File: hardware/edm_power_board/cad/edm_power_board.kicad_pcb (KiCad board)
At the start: 4 copper layers, 240 x 100 mm, 158 parts, among them J501 Conn_02x08_Odd_Even, J502 Conn_01x02, Q201 SUD19P06-60, Q301 BSS214NW, Q302 BSC13DN30NSFD, Q303 BSS214NW, Q304 BSS214NW, Q601 IPD50R3K0CE, Q602 IPD50R380CE, U201 LM358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

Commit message: Update bleed resistor
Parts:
- removed MK506, MK512: Mounting_Hole_PAD, MountingHole:MountingHole_5mm_Pad
- added R623: 187k, Resistor_SMD:R_0805_2012Metric, F.Cu at (225.0, -9.96)
- added R624: 187k, Resistor_SMD:R_0805_2012Metric, F.Cu at (225.0, -6.04)
- C315, C316: value 25u -> 470n; footprint Capacitor_THT:C_Rect_L41.5mm_W20.0mm_P37.50mm_MKS4 -> Capacitor_SMD:C_1812_4532Metric
- R308, R316: value 261R -> 26k1
- R313: value 523R -> 52k3
- R317: value 21k -> 2M1
- R318: value 180R -> 18k
- R612, R618: value 10k -> 21k
- R613, R614, R619, R620: value 93k1 -> 187k
- RV601: value 50k -> 100k
- RV602: value 250k -> 500k
- moved C316 22.0 mm to (137.0, -63.8), turned to 270 degrees
- moved C315 21.2 mm to (131.0, -63.8), turned to 270 degrees
- moved R216 2.00 mm to (158.9, -30.0)
- moved R220 2.00 mm to (166.6, -30.0)
- moved R221 2.00 mm to (162.7, -30.0)
- moved C602 2.00 mm to (182.3, -14.2)
- moved C608 2.00 mm to (114.7, -6.37)
- moved C201 2.00 mm to (155.2, -30.0)
- moved C202 2.00 mm to (147.6, -29.9)
- moved C203 2.00 mm to (141.7, -42.4)
- moved C204 2.00 mm to (147.0, -43.2)
- moved C205 2.00 mm to (142.3, -29.3)
- moved C206 2.00 mm to (146.5, -23.0)
- moved C207 2.00 mm to (148.9, -37.5)
- moved C208 2.00 mm to (155.2, -37.5)
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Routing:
- net GNDPWR: track 212.4 -> 232.3 mm, vias 108 -> 117
- net Net-(R623-Pad1): track 0.00 -> 2.00 mm
- net Net-(C310-Pad2): track 0.00 -> 1.59 mm
- net Net-(Q304-Pad1): track 65.1 -> 64.3 mm
- net Net-(R304-Pad2): track 86.6 -> 85.8 mm
- net +5V: track 165.8 -> 165.0 mm
- net Net-(U601-Pad14): track 185.6 -> 184.8 mm
- net Net-(U601-Pad13): track 152.7 -> 151.8 mm
- net Net-(R615-Pad1): track 74.7 -> 73.8 mm
- net Net-(R606-Pad1): track 97.5 -> 96.7 mm
- net Net-(Q303-Pad1): track 64.4 -> 63.6 mm
- net Net-(Q301-Pad1): track 63.9 -> 63.1 mm
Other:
- board size 240 x 100 mm -> 240 x 80 mm

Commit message: Rotate board
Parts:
- removed MK505, MK511: Mounting_Hole_PAD, MountingHole:MountingHole_5mm_Pad
- moved MK501 235.0 mm to (234.4, -63.8), turned to 180 degrees
- moved MK507 235.0 mm to (5.60, -63.8), turned to 180 degrees
- moved MK504 232.6 mm to (234.4, -16.2), turned to 180 degrees
- moved MK510 232.6 mm to (5.60, -16.2), turned to 180 degrees
- moved MK502 229.8 mm to (234.4, -47.9), turned to 180 degrees
- moved MK508 229.8 mm to (5.60, -47.9), turned to 180 degrees
- moved MK503 229.0 mm to (234.4, -32.1), turned to 180 degrees
- moved MK509 229.0 mm to (5.60, -32.1), turned to 180 degrees
- moved R624 220.7 mm to (15.0, -74.0), turned to 270 degrees
- moved R623 218.4 mm to (15.0, -70.0), turned to 270 degrees
- moved JJ503 207.2 mm to (20.0, -13.0), turned to 0 degrees
- moved D607 200.8 mm to (23.0, -66.0), turned to 0 degrees
- moved R619 193.2 mm to (30.0, -75.0), turned to 180 degrees
- moved J501 192.4 mm to (215.5, -51.4), turned to 180 degrees
- moved R613 191.1 mm to (30.0, -72.0), turned to 180 degrees
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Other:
- outline, holes or cut-outs redrawn
- board text added: "+24V"
- board text added: "0V"
- board text added: "1"
- board text added: "Breakdown"
- board text added: "Out+"
- board text added: "Out-"
- board text added: "Short circuit"
- board text added: "Spark voltage"

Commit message: Routing
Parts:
- added C501: 1800p, Capacitor_SMD:C_2220_5650Metric, F.Cu at (220.5, -16.0)
- added R501: 1M, Resistor_SMD:R_1206_3216Metric, F.Cu at (220.5, -24.0)
- moved R623 3.16 mm to (18.0, -71.0)
- moved R624 3.16 mm to (18.0, -75.0)
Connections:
- MK501 pad 1: GNDPWR -> /Connectors/Shield
- MK502 pad 1: GNDPWR -> /Connectors/Shield
- MK503 pad 1: GNDPWR -> /Connectors/Shield
- MK504 pad 1: GNDPWR -> /Connectors/Shield
- MK507 pad 1: GNDPWR -> /Connectors/Shield
- MK508 pad 1: GNDPWR -> /Connectors/Shield
- MK509 pad 1: GNDPWR -> /Connectors/Shield
- MK510 pad 1: GNDPWR -> /Connectors/Shield
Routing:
- net /Connectors/Shield: track 0.00 -> 27.1 mm
- net GNDPWR: track 232.3 -> 246.2 mm, vias 117 -> 121
- added copper zone on B.Cu, net /Connectors/Shield
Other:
- board text added: "EDM Power Board 2018-02-18 JS"
- board text added: "EDM current"
- board text removed: "Spark voltage"

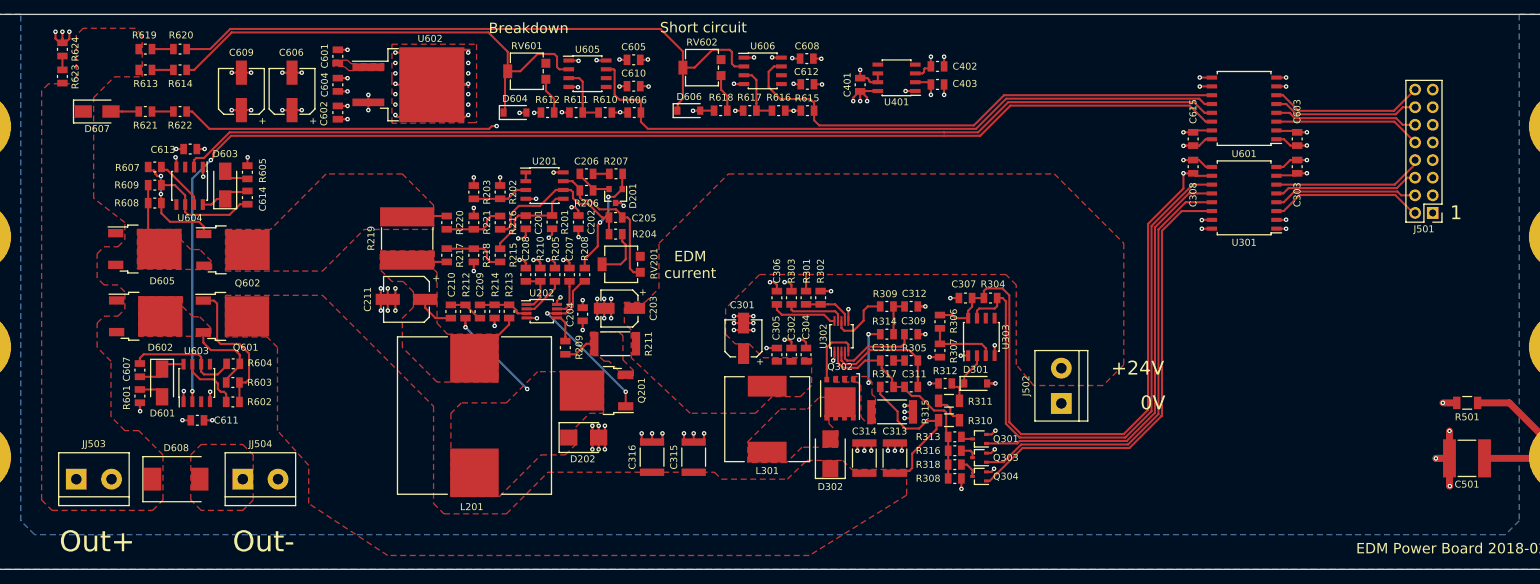
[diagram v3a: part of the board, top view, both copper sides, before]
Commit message: Added copper planes to front and back. Added gerber files.
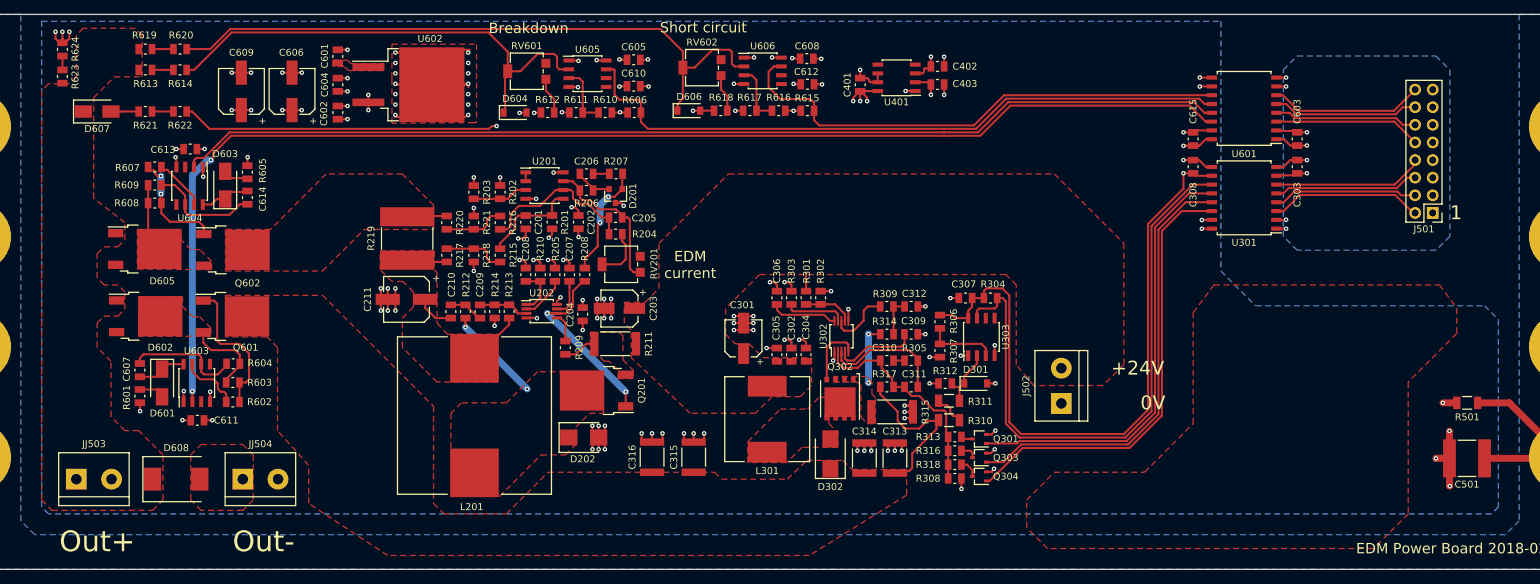
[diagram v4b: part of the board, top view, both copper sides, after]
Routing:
- added copper zone on F.Cu, net (none)
- added copper zone on B.Cu, net GND
- added copper zone on B.Cu, net GNDPWR
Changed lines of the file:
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@@
     (thickness 1.6)
     (drawings 13)
-    (tracks 1160)
+    (tracks 1161)
     (zones 0)
     (modules 158)
@@
     (31 B.Cu signal hide)
     (32 B.Adhes user hide)
-    (33 F.Adhes user)
-    (34 B.Paste user)
-    (35 F.Paste user)
-    (36 B.SilkS user)
-    (37 F.SilkS user)
-    (38 B.Mask user)
-    (39 F.Mask user)
-    (40 Dwgs.User user)
-    (41 Cmts.User user)
-    (42 Eco1.User user)
-    (43 Eco2.User user)
+    (33 F.Adhes user hide)
+    (34 B.Paste user hide)
+    (35 F.Paste user hide)
+    (36 B.SilkS user hide)
+    (37 F.SilkS user hide)
+    (38 B.Mask user hide)
+    (39 F.Mask user hide)
+    (40 Dwgs.User user hide)
+    (41 Cmts.User user hide)
+    (42 Eco1.User user hide)
+    (43 Eco2.User user hide)
     (44 Edge.Cuts user)
-    (45 Margin user)
-    (46 B.CrtYd user)
-    (47 F.CrtYd user)
-    (48 B.Fab user)
-    (49 F.Fab user)
+    (45 Margin user hide)
+    (46 B.CrtYd user hide)
+    (47 F.CrtYd user hide)
+    (48 B.Fab user hide)
+    (49 F.Fab user hide)
   )
   (setup
@@
       (outputformat 1)
       (mirror false)
-      (drillshape 1)
+      (drillshape 0)
       (scaleselection 1)
-      (outputdirectory ""))
+      (outputdirectory ../documents/gerber/))
   )
   (net 0 "")
@@
   (segment (start 37.3 -59.3) (end 36.966965 -58.966965) (width 0.3) (layer F.Cu) (net 30))
   (segment (start 36.966965 -58.966965) (end 36.966965 -57.988462) (width 0.3) (layer F.Cu) (net 30))
+  (segment (start 39.4 -59) (end 38.940381 -59) (width 1) (layer B.Cu) (net 31))
+  (segment (start 38.940381 -59) (end 36.72999 -56.789609) (width 1) (layer B.Cu) (net 31))
+  (segment (start 36.72999 -56.789609) (end 36.72999 -26.129629) (width 1) (layer B.Cu) (net 31))
+  (segment (start 36.72999 -26.129629) (end 36.72999 -25.67001) (width 1) (layer B.Cu) (net 31))
   (segment (start 154.64997 -66.84997) (end 180.5 -66.84997) (width 0.3) (layer F.Cu) (net 31))
   (segment (start 145.10001 -62.49999) (end 150.29999 -62.49999) (width 0.3) (layer F.Cu) (net 31))
@@
   (via (at 39.4 -59) (size 0.65) (drill 0.3) (layers F.Cu B.Cu) (net 31))
   (via (at 36.72999 -25.67001) (size 0.65) (drill 0.3) (layers F.Cu B.Cu) (net 31))
-  (segment (start 36.72999 -25.67001) (end 36.72999 -56.32999) (width 0.3) (layer B.Cu) (net 31))
-  (segment (start 36.72999 -56.32999) (end 39.4 -59) (width 0.3) (layer B.Cu) (net 31))
   (segment (start 36.72999 -24.173646) (end 36.72999 -25.67001) (width 0.3) (layer F.Cu) (net 31))
   (segment (start 128.700183 -35.799817) (end 127.8 -36.7) (width 0.3) (layer F.Cu) (net 42))
@@
   (segment (start 144.5 -23.7) (end 144.3 -23.9) (width 0.3) (layer F.Cu) (net 53))
   (segment (start 144.3 -23.9) (end 144.3 -24.3) (width 0.3) (layer F.Cu) (net 53))
+  (segment (start 87.9 -36.9) (end 99.2 -25.6) (width 1) (layer B.Cu) (net 61))
   (segment (start 83.734606 -50.998433) (end 83.2 -50.463827) (width 0.3) (layer F.Cu) (net 63))
   (segment (start 84.784606 -50.998433) (end 83.734606 -50.998433) (width 0.3) (layer F.Cu) (net 63))
@@
   (segment (start 89.122173 -54.687481) (end 86.834692 -52.4) (width 0.3) (layer F.Cu) (net 65))
   (segment (start 82.122481 -49.022481) (end 81.097173 -49.022481) (width 0.3) (layer F.Cu) (net 65))
+  (segment (start 95.5 -50) (end 95.5 -52.5) (width 1) (layer B.Cu) (net 70))
+  (segment (start 95.5 -52.5) (end 96.7 -53.7) (width 1) (layer B.Cu) (net 70))
+  (segment (start 76.1 -34.9) (end 85 -26) (width 1) (layer B.Cu) (net 71))
   (segment (start 32.666965 -57.6) (end 33.1 -57.6) (width 0.3) (layer F.Cu) (net 80))
   (segment (start 32.266965 -58) (end 32.666965 -57.6) (width 0.3) (layer F.Cu) (net 80))
   (segment (start 33.1 -57.6) (end 36.966965 -53.733035) (width 0.3) (layer F.Cu) (net 80))
   (segment (start 36.966965 -53.733035) (end 36.966965 -52.588462) (width 0.3) (layer F.Cu) (net 80))
+  (segment (start 32.2 -56.7) (end 32.2 -54.1) (width 1) (layer B.Cu) (net 81))
   (segment (start 31.4 -57) (end 31.7 -56.7) (width 0.3) (layer F.Cu) (net 81))
   (segment (start 31.7 -56.7) (end 32.2 -56.7) (width 0.3) (layer F.Cu) (net 81))
@@
   (segment (start 32.2 -54.1) (end 32.2 -53.055427) (width 0.3) (layer F.Cu) (net 81))
   (segment (start 32.2 -53.055427) (end 32.266965 -52.988462) (width 0.3) (layer F.Cu) (net 81))
-  (segment (start 32.2 -56.7) (end 32.2 -54.1) (width 0.3) (layer B.Cu) (net 81))
   (via (at 32.2 -54.1) (size 0.65) (drill 0.3) (layers F.Cu B.Cu) (net 81))
   (via (at 32.2 -56.7) (size 0.65) (drill 0.3) (layers F.Cu B.Cu) (net 81))
@@
   (segment (start 26.55 -66) (end 29 -66) (width 0.3) (layer F.Cu) (net 90))
   (segment (start 30.91 -66) (end 34 -66) (width 0.3) (layer F.Cu) (net 91))
-  (segment (start 134.200001 -26.9) (end 134.200001 -33.899993) (width 0.3) (layer B.Cu) (net 93))
-  (segment (start 134.200001 -33.899993) (end 134.200008 -33.9) (width 0.3) (layer B.Cu) (net 93))
+  (segment (start 134.200001 -26.9) (end 134.200001 -33.899993) (width 1) (layer B.Cu) (net 93))
+  (segment (start 134.200001 -33.899993) (end 134.200008 -33.9) (width 1) (layer B.Cu) (net 93))
   (segment (start 134.200191 -33.899817) (end 134.200008 -33.9) (width 0.3) (layer F.Cu) (net 93))
   (segment (start 135.896959 -33.899817) (end 134.200191 -33.899817) (width 0.3) (layer F.Cu) (net 93))
@@
   (segment (start 99.2 -23.5) (end 99.2 -25.6) (width 0.3) (layer F.Cu) (net 61))
   (via (at 99.2 -25.6) (size 0.65) (drill 0.3) (layers F.Cu B.Cu) (net 61))
-  (segment (start 99.2 -25.6) (end 87.9 -36.9) (width 0.3) (layer B.Cu) (net 61))
   (segment (start 87.9 -36.9) (end 89.294654 -36.9) (width 0.3) (layer F.Cu) (net 61))
   (segment (start 89.294654 -36.9) (end 89.297173 -36.897481) (width 0.3) (layer F.Cu) (net 61))
@@
   (segment (start 95.175001 -46.575001) (end 95.175001 -49.675001) (width 0.3) (layer F.Cu) (net 70))
   (segment (start 95.175001 -49.675001) (end 95.5 -50) (width 0.3) (layer F.Cu) (net 70))
-  (segment (start 96.7 -53.7) (end 96.7 -51.2) (width 0.3) (layer B.Cu) (net 70))
-  (segment (start 96.7 -51.2) (end 95.824999 -50.324999) (width 0.3) (layer B.Cu) (net 70))
-  (segment (start 95.824999 -50.324999) (end 95.5 -50) (width 0.3) (layer B.Cu) (net 70))
   (via (at 95.5 -50) (size 0.65) (drill 0.3) (layers F.Cu B.Cu) (net 70))
   (segment (start 96.7 -53.7) (end 97.574692 -53.7) (width 0.3) (layer F.Cu) (net 70))
@@
   (segment (start 98.697173 -56.967481) (end 98.752173 -57.022481) (width 0.3) (layer F.Cu) (net 70))
   (segment (start 85 -26) (end 85.000004 -26) (width 0.3) (layer B.Cu) (net 71))
-  (segment (start 76.1 -34.9) (end 85 -26) (width 0.3) (layer B.Cu) (net 71))
   (via (at 85 -26) (size 0.65) (drill 0.3) (layers F.Cu B.Cu) (net 71))
   (segment (start 92.88 -25.8) (end 92.9 -25.78) (width 0.3) (layer F.Cu) (net 71))
@@
       )
     )
+  )
+  (zone (net 0) (net_name "") (layer F.Cu) (hatch edge 0.508)
+    (connect_pads (clearance 0.508))
+    (min_thickness 0.254)
+    (fill yes (arc_segments 16) (thermal_gap 0.508) (thermal_bridge_width 0.508))
+    (polygon
+      (pts
+        (xy 157 -6) (xy 157 -10) (xy 161 -14) (xy 174 -14) (xy 181 -21)
+        (xy 181 -37) (xy 184 -41) (xy 216.500002 -41) (xy 219 -37.666667) (xy 219 -34)
+        (xy 212 -27) (xy 212 -8) (xy 207 -3) (xy 160 -3)
+      )
+    )
+  )
+  (zone (net 1) (net_name GNDPWR) (layer B.Cu) (hatch edge 0.508)
+    (connect_pads (clearance 0.508))
+    (min_thickness 0.254)
+    (fill yes (arc_segments 16) (thermal_gap 0.508) (thermal_bridge_width 0.508))
+    (polygon
+      (pts
+        (xy 185 -43) (xy 190 -38) (xy 223 -38) (xy 225 -36) (xy 225 -9)
+        (xy 224 -8) (xy 16 -8) (xy 15 -9) (xy 15 -79) (xy 185 -79)
+      )
+    )
+  )
+  (zone (net 3) (net_name GND) (layer B.Cu) (hatch edge 0.508)
+    (connect_pads yes (clearance 0.508))
+    (min_thickness 0.254)
+    (fill yes (arc_segments 16) (thermal_gap 0.508) (thermal_bridge_width 0.508))
+    (polygon
+      (pts
+        (xy 218 -48) (xy 216 -46) (xy 196 -46) (xy 194 -48) (xy 194 -72)
+        (xy 196 -74) (xy 216 -74) (xy 218 -72)
+      )
+    )
